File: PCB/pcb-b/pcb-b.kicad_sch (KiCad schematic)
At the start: 24 parts, among them J1 Conn_02x05_Counter_Clockwise, J2 Conn_02x04_Counter_Clockwise, K1 HK19F-DCxxV-SHC, Q13 TPCA8120,L1Q, Q3 BC817, Q9 BC817

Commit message: Fixes
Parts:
- removed J2: Conn_02x04_Counter_Clockwise, Connector_PinHeader_2.54mm:PinHeader_2x04_P2.54mm_Vertical, symbol Connector_Generic:Conn_02x04_Counter_Clockwise
- added J2: Conn_02x05_Counter_Clockwise, Connector_PinHeader_2.54mm:PinHeader_2x05_P2.54mm_Vertical, symbol Connector_Generic:Conn_02x05_Counter_Clockwise
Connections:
- net c_engineOFF: now also J2.7 (Pin_7)
- net c_leftArrow: now also J2.3 (Pin_3)
- net c_rightArrow: now also J2.2 (Pin_2)
- net o_engineON: now also J2.4 (Pin_4)
- net o_engineReady: now also J2.8 (Pin_8)
- net o_keepAlive: now also J2.9 (Pin_9)
- net o_neutral: now also J2.10 (Pin_10)
- no-connect marks 4 -> 6
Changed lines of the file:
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@@
 	)
 	(no_connect
+		(at 119.888 82.55)
+	)
+	(no_connect
 		(at 199.644 110.236)
 	)
@@
 	)
 	(no_connect
+		(at 132.588 82.55)
+	)
+	(no_connect
 		(at 199.644 100.076)
 	)
@@
 	)
 	(symbol
-		(lib_id "Connector_Generic:Conn_02x04_Counter_Clockwise")
-		(at 124.968 74.93 0)
-		(unit 1)
-		(exclude_from_sim no)
-		(in_bom yes)
-		(on_board yes)
-		(dnp no)
-		(property "Reference" "J2"
-			(at 126.492 82.804 0)
-			(effects
-				(font
-					(size 1.27 1.27)
-				)
-			)
-		)
-		(property "Value" "Conn_02x04_Counter_Clockwise"
-			(at 126.238 69.088 0)
-			(effects
-				(font
-					(size 1.27 1.27)
-				)
-				(hide yes)
-			)
-		)
-		(property "Footprint" "Connector_PinHeader_2.54mm:PinHeader_2x04_P2.54mm_Vertical"
-			(at 124.968 74.93 0)
-			(effects
-				(font
-					(size 1.27 1.27)
-				)
-				(hide yes)
-			)
-		)
-		(property "Datasheet" "~"
-			(at 124.968 74.93 0)
-			(effects
-				(font
-					(size 1.27 1.27)
-				)
-				(hide yes)
-			)
-		)
-		(property "Description" "Generic connector, double row, 02x04, counter clockwise pin numbering scheme (similar to DIP package numbering), script generated (kicad-library-utils/schlib/autogen/connector/)"
-			(at 124.968 74.93 0)
-			(effects
-				(font
-					(size 1.27 1.27)
-				)
-				(hide yes)
-			)
-		)
-		(pin "8"
-		)
-		(pin "7"
-		)
-		(pin "1"
-		)
-		(pin "6"
-		)
-		(pin "5"
-		)
-		(pin "4"
-		)
-		(pin "3"
-		)
-		(pin "2"
-		)
-		(instances
-			(project ""
-				(path "/709d0967-afe5-49d3-92a5-d2bb94550bdb"
-					(reference "J2")
-					(unit 1)
-				)
-			)
-		)
-	)
-	(symbol
 		(lib_id "Device:R")
 		(at 246.634 114.046 0)
@@
 					(unit 1)
 				)
+			)
+		)
+	)
+	(symbol
+		(lib_id "Connector_Generic:Conn_02x05_Counter_Clockwise")
+		(at 124.968 77.47 0)
+		(unit 1)
+		(exclude_from_sim no)
+		(in_bom yes)
+		(on_board yes)
+		(dnp no)
+		(property "Reference" "J2"
+			(at 126.238 69.342 0)
+			(effects
+				(font
+					(size 1.27 1.27)
+				)
+			)
+		)
+		(property "Value" "Conn_02x05_Counter_Clockwise"
+			(at 126.238 68.834 0)
+			(effects
+				(font
+					(size 1.27 1.27)
+				)
+				(hide yes)
+			)
+		)
+		(property "Footprint" "Connector_PinHeader_2.54mm:PinHeader_2x05_P2.54mm_Vertical"
+			(at 124.968 77.47 0)
+			(effects
+				(font
+					(size 1.27 1.27)
+				)
+				(hide yes)
+			)
+		)
+		(property "Datasheet" "~"
+			(at 124.968 77.47 0)
+			(effects
+				(font
+					(size 1.27 1.27)
+				)
+				(hide yes)
+			)
+		)
+		(property "Description" "Generic connector, double row, 02x05, counter clockwise pin numbering scheme (similar to DIP package numbering), script generated (kicad-library-utils/schlib/autogen/connector/)"
+			(at 124.968 77.47 0)
+			(effects
+				(font
+					(size 1.27 1.27)
+				)
+				(hide yes)
+			)
+		)
+		(pin "6"
+		)
+		(pin "8"
+		)
+		(pin "2"
+		)
+		(pin "5"
+		)
+		(pin "3"
+		)
+		(pin "4"
+		)
+		(pin "10"
+		)
+		(pin "1"
+		)
+		(pin "7"
+		)
+		(pin "9"
+		)
+		(instances
+			(project "pcb-b"
+				(path "/709d0967-afe5-49d3-92a5-d2bb94550bdb"
+					(reference "J2")
+					(unit 1)
+				)

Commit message: Footprint updating
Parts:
- Q13: footprint TPCA8120:TPH4R003NLL1Q -> TPCA80120:TPH4R003NLL1Q
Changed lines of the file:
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@@
 			)
 		)
-		(property "Footprint" "TPCA8120:TPH4R003NLL1Q"
+		(property "Footprint" "TPCA80120:TPH4R003NLL1Q"
 			(at 92.202 195.25 0)
 			(effects

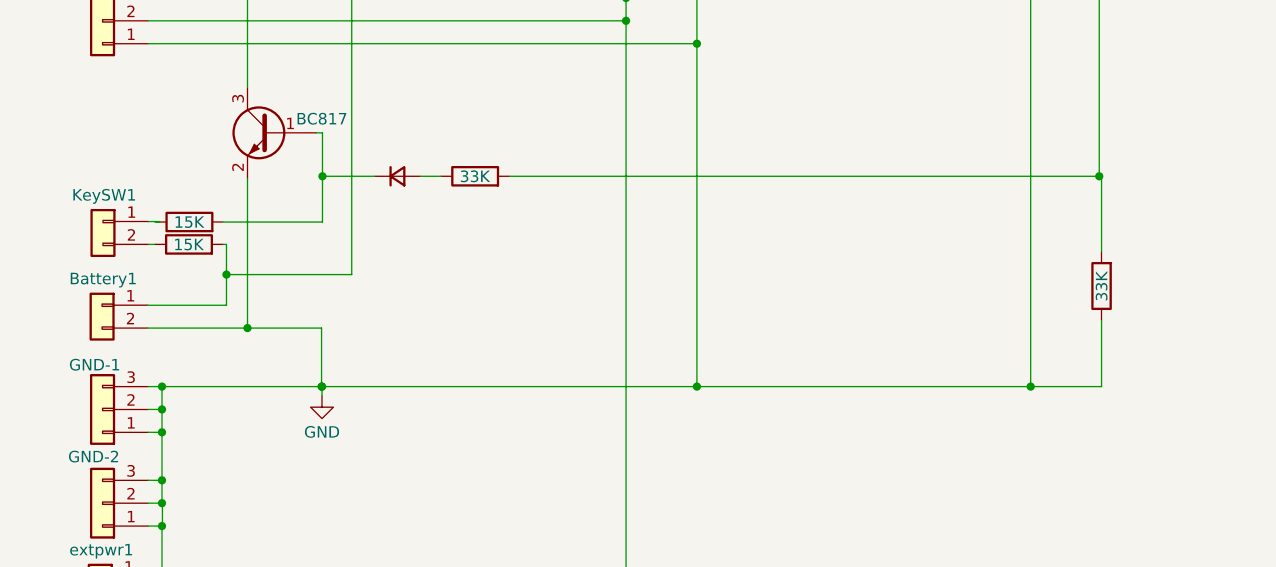
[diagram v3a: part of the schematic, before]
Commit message: Floating BC817's base fixed
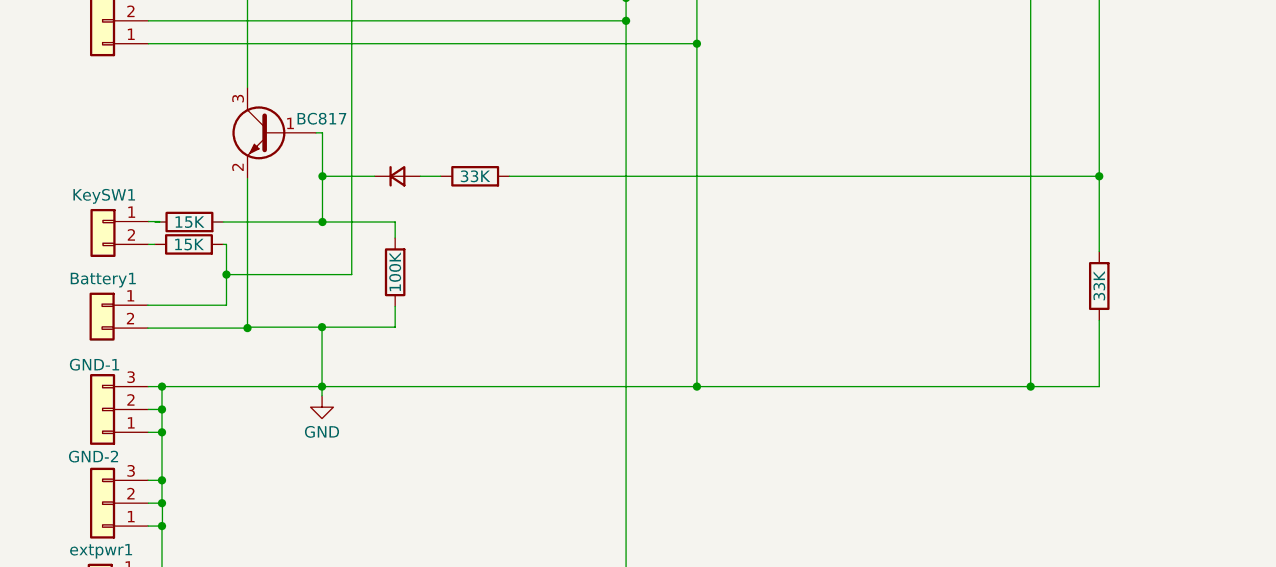
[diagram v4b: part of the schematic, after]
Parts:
- added R7: 100K, Resistor_SMD:R_1206_3216Metric, symbol Device:R
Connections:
- net GND: now also R7.1
- net at D1.1 (K), Q9.1 (B), R4.2: now also R7.2
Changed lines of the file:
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@@
+	)
+	(junction
+		(at 63.5508 140.462)
+		(diameter 0)
+		(color 0 0 0 0)
 	)
 	(junction
@@
 	)
 	(junction
-		(at 63.4492 158.75)
-		(diameter 0)
-		(color 0 0 0 0)
-	)
-	(junction
 		(at 105.156 120.65)
 		(diameter 0)
@@
 	)
 	(junction
+		(at 63.5 152.146)
+		(diameter 0)
+		(color 0 0 0 0)
+	)
+	(junction
 		(at 97.282 118.11)
 		(diameter 0)
@@
 	(wire
 		(pts
-			(xy 150.114 135.382) (xy 150.114 143.764)
+			(xy 149.86 135.382) (xy 149.86 143.764)
 		)
 		(stroke
@@
 	(wire
 		(pts
+			(xy 55.2704 152.2476) (xy 55.2196 152.2476)
+		)
+		(stroke
+			(width 0)
+			(type default)
+		)
+	)
+	(wire
+		(pts
 			(xy 138.684 77.978) (xy 138.684 77.47)
 		)
@@
 	(wire
 		(pts
-			(xy 45.72 158.75) (xy 63.4492 158.75)
+			(xy 45.72 158.75) (xy 63.5 158.75)
 		)
 		(stroke
@@
 	(wire
 		(pts
-			(xy 55.2196 152.2476) (xy 63.4492 152.2476)
+			(xy 55.2704 152.146) (xy 63.5 152.146)
 		)
 		(stroke
@@
 	(wire
 		(pts
+			(xy 63.5 152.146) (xy 71.628 152.146)
+		)
+		(stroke
+			(width 0)
+			(type default)
+		)
+	)
+	(wire
+		(pts
 			(xy 147.574 80.772) (xy 147.574 80.01)
 		)
@@
 	(wire
 		(pts
-			(xy 150.114 135.382) (xy 149.86 135.382)
-		)
-		(stroke
-			(width 0)
-			(type default)
-		)
-	)
-	(wire
-		(pts
 			(xy 66.802 96.2152) (xy 67.056 96.2152)
 		)
@@
 	(wire
 		(pts
-			(xy 63.4492 152.2476) (xy 63.4492 158.75)
+			(xy 63.5 152.146) (xy 63.5 158.75)
 		)
 		(stroke
@@
 	(wire
 		(pts
-			(xy 142.24 158.75) (xy 150.114 158.75)
+			(xy 142.24 158.75) (xy 149.86 158.75)
 		)
 		(stroke
@@
 	(wire
 		(pts
-			(xy 63.4492 158.75) (xy 63.5 158.75)
+			(xy 55.2704 152.146) (xy 55.2704 152.2476)
+		)
+		(stroke
+			(width 0)
+			(type default)
+		)
+	)
+	(wire
+		(pts
+			(xy 71.628 142.24) (xy 71.628 140.462)
 		)
 		(stroke
@@
 	(wire
 		(pts
+			(xy 63.5508 140.462) (xy 71.628 140.462)
+		)
+		(stroke
+			(width 0)
+			(type default)
+		)
+	)
+	(wire
+		(pts
 			(xy 70.5612 100.33) (xy 70.5612 102.87)
 		)
@@
 	(wire
 		(pts
-			(xy 150.114 151.384) (xy 150.114 158.75)
+			(xy 149.86 151.384) (xy 149.86 158.75)
 		)
 		(stroke
@@
 		(pts
 			(xy 149.86 75.184) (xy 149.86 135.382)
+		)
+		(stroke
+			(width 0)
+			(type default)
+		)
+	)
+	(wire
+		(pts
+			(xy 71.628 152.146) (xy 71.628 149.86)
 		)
 		(stroke
@@
 	(symbol
 		(lib_id "Device:R")
+		(at 71.628 146.05 180)
+		(unit 1)
+		(exclude_from_sim no)
+		(in_bom yes)
+		(on_board yes)
+		(dnp no)
+		(property "Reference" "R7"
+			(at 65.3288 146.05 90)
+			(effects
+				(font
+					(size 1.27 1.27)
+				)
+				(hide yes)
+			)
+		)
+		(property "Value" "100K"
+			(at 71.6788 146.1008 90)
+			(effects
+				(font
+					(size 1.27 1.27)
+				)
+			)
+		)
+		(property "Footprint" "Resistor_SMD:R_1206_3216Metric"
+			(at 73.406 146.05 90)
+			(effects
+				(font
+					(size 1.27 1.27)
+				)
+				(hide yes)
+			)
+		)
+		(property "Datasheet" "~"
+			(at 71.628 146.05 0)
+			(effects
+				(font
+					(size 1.27 1.27)
+				)
+				(hide yes)
+			)
+		)
+		(property "Description" ""
+			(at 71.628 146.05 0)
+			(effects
+				(font
+					(size 1.27 1.27)
+				)
+				(hide yes)
+			)
+		)
+		(pin "1"
+		)
+		(pin "2"
+		)
+		(instances
+			(project "pcb-b"
+				(path "/709d0967-afe5-49d3-92a5-d2bb94550bdb"
+					(reference "R7")
+					(unit 1)
+				)
+			)
+		)
+	)
+	(symbol
+		(lib_id "Device:R")
 		(at 48.7172 142.9512 90)
 		(unit 1)
@@
 	(symbol
 		(lib_id "Device:R")
-		(at 150.114 147.574 180)
+		(at 149.86 147.574 180)
 		(unit 1)
 		(exclude_from_sim no)
@@
 		(dnp no)
 		(property "Reference" "R6"
-			(at 143.8148 147.574 90)
+			(at 143.5608 147.574 90)
 			(effects
 				(font
@@
 		)
 		(property "Value" "33K"
-			(at 150.1648 147.6248 90)
+			(at 149.9108 147.6248 90)
 			(effects
 				(font
@@
 		)
 		(property "Footprint" "Resistor_SMD:R_1206_3216Metric"
-			(at 151.892 147.574 90)
+			(at 151.638 147.574 90)
 			(effects
 				(font
@@
 		)
 		(property "Datasheet" "~"
-			(at 150.114 147.574 0)
+			(at 149.86 147.574 0)
 			(effects
 				(font
@@
 		)
 		(property "Description" ""
-			(at 150.114 147.574 0)
-			(effects
-				(font
+			(at 149.86 147.574 0)
+			(effects
+				(font

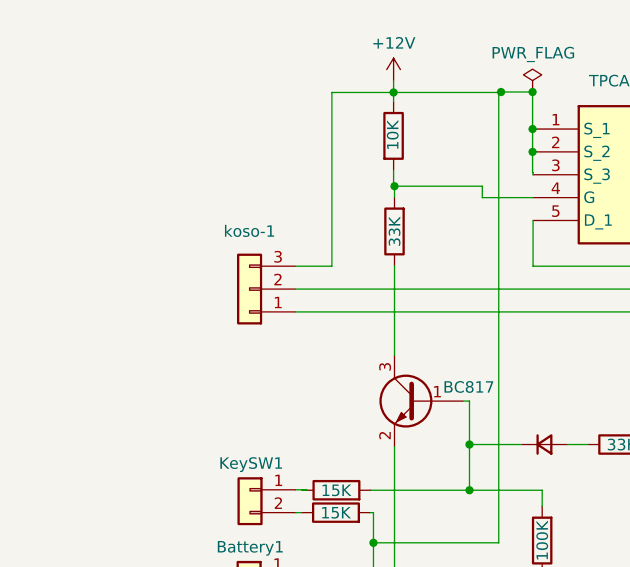
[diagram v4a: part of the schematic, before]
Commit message: Components sizes and positions optimizing
- 3-pins Koso's comnnector has been substituted with a more standard 4-pins one
- One resistor has been moved to free space for EngReady_led connector
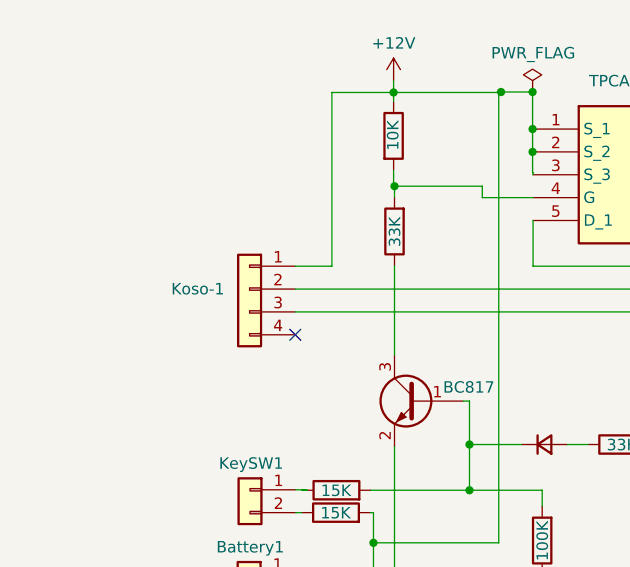
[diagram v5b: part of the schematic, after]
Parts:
- removed koso-1: Conn_01x03, Connector_PinHeader_2.54mm:PinHeader_1x03_P2.54mm_Vertical, symbol Connector_Generic:Conn_01x03
- added Koso-1: Conn_01x04, Connector_PinHeader_2.54mm:PinHeader_1x04_P2.54mm_Vertical, symbol Connector_Generic:Conn_01x04
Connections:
- net +12V: now also Koso-1.1 (Pin_1)
- net GND: now also Koso-1.3 (Pin_3)
- net tempPower: now also Koso-1.2 (Pin_2)
- no-connect marks 6 -> 7
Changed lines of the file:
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@@
 	)
 	(no_connect
+		(at 44.196 123.19)
+	)
+	(no_connect
 		(at 119.888 72.39)
 	)
@@
 	)
 	(symbol
+		(lib_id "Connector_Generic:Conn_01x04")
+		(at 39.116 118.11 0)
+		(mirror y)
+		(unit 1)
+		(exclude_from_sim no)
+		(in_bom yes)
+		(on_board yes)
+		(dnp no)
+		(property "Reference" "Koso-1"
+			(at 36.322 118.1099 0)
+			(effects
+				(font
+					(size 1.27 1.27)
+				)
+				(justify left)
+			)
+		)
+		(property "Value" "Conn_01x04"
+			(at 36.322 120.6499 0)
+			(effects
+				(font
+					(size 1.27 1.27)
+				)
+				(justify left)
+				(hide yes)
+			)
+		)
+		(property "Footprint" "Connector_PinHeader_2.54mm:PinHeader_1x04_P2.54mm_Vertical"
+			(at 39.116 118.11 0)
+			(effects
+				(font
+					(size 1.27 1.27)
+				)
+				(hide yes)
+			)
+		)
+		(property "Datasheet" "~"
+			(at 39.116 118.11 0)
+			(effects
+				(font
+					(size 1.27 1.27)
+				)
+				(hide yes)
+			)
+		)
+		(property "Description" "Generic connector, single row, 01x04, script generated (kicad-library-utils/schlib/autogen/connector/)"
+			(at 39.116 118.11 0)
+			(effects
+				(font
+					(size 1.27 1.27)
+				)
+				(hide yes)
+			)
+		)
+		(pin "2"
+		)
+		(pin "3"
+		)
+		(pin "1"
+		)
+		(pin "4"
+		)
+		(instances
+			(project ""
+				(path "/709d0967-afe5-49d3-92a5-d2bb94550bdb"
+					(reference "Koso-1")
+					(unit 1)
+				)
+			)
+		)
+	)
+	(symbol
 		(lib_id "power:GND")
 		(at 197.104 115.316 0)
@@
 					(unit 1)
 				)
-			)
-		)
-	)
-	(symbol
-		(lib_id "Connector_Generic:Conn_01x03")
-		(at 39.116 118.11 180)
-		(unit 1)
-		(exclude_from_sim no)
-		(in_bom yes)
-		(on_board yes)
-		(dnp no)
-		(property "Reference" "koso-1"
-			(at 39.116 111.7092 0)
-			(effects
-				(font
-					(size 1.27 1.27)
-				)
-			)
-		)
-		(property "Value" "Conn_01x03"
-			(at 35.9156 116.8401 0)
-			(effects
-				(font
-					(size 1.27 1.27)
-				)
-				(justify left)
-				(hide yes)
-			)
-		)
-		(property "Footprint" "Connector_PinHeader_2.54mm:PinHeader_1x03_P2.54mm_Vertical"
-			(at 39.116 118.11 0)
-			(effects
-				(font
-					(size 1.27 1.27)
-				)
-				(hide yes)
-			)
-		)
-		(property "Datasheet" "~"
-			(at 39.116 118.11 0)
-			(effects
-				(font
-					(size 1.27 1.27)
-				)
-				(hide yes)
-			)
-		)
-		(property "Description" ""
-			(at 39.116 118.11 0)
-			(effects
-				(font
-					(size 1.27 1.27)
-				)
-				(hide yes)
-			)
-		)
-		(pin "1"
-		)
-		(pin "2"
-		)
-		(pin "3"
-		)
-		(instances
-			(project "pcb-b"
-				(path "/709d0967-afe5-49d3-92a5-d2bb94550bdb"
-					(reference "koso-1")
-					(unit 1)
-				)
